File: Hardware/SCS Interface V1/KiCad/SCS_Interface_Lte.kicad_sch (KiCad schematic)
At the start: 23 parts, among them J1 SCS, J2 Conn_01x04, Q1 MMBTA06, Q2 MMBTA06

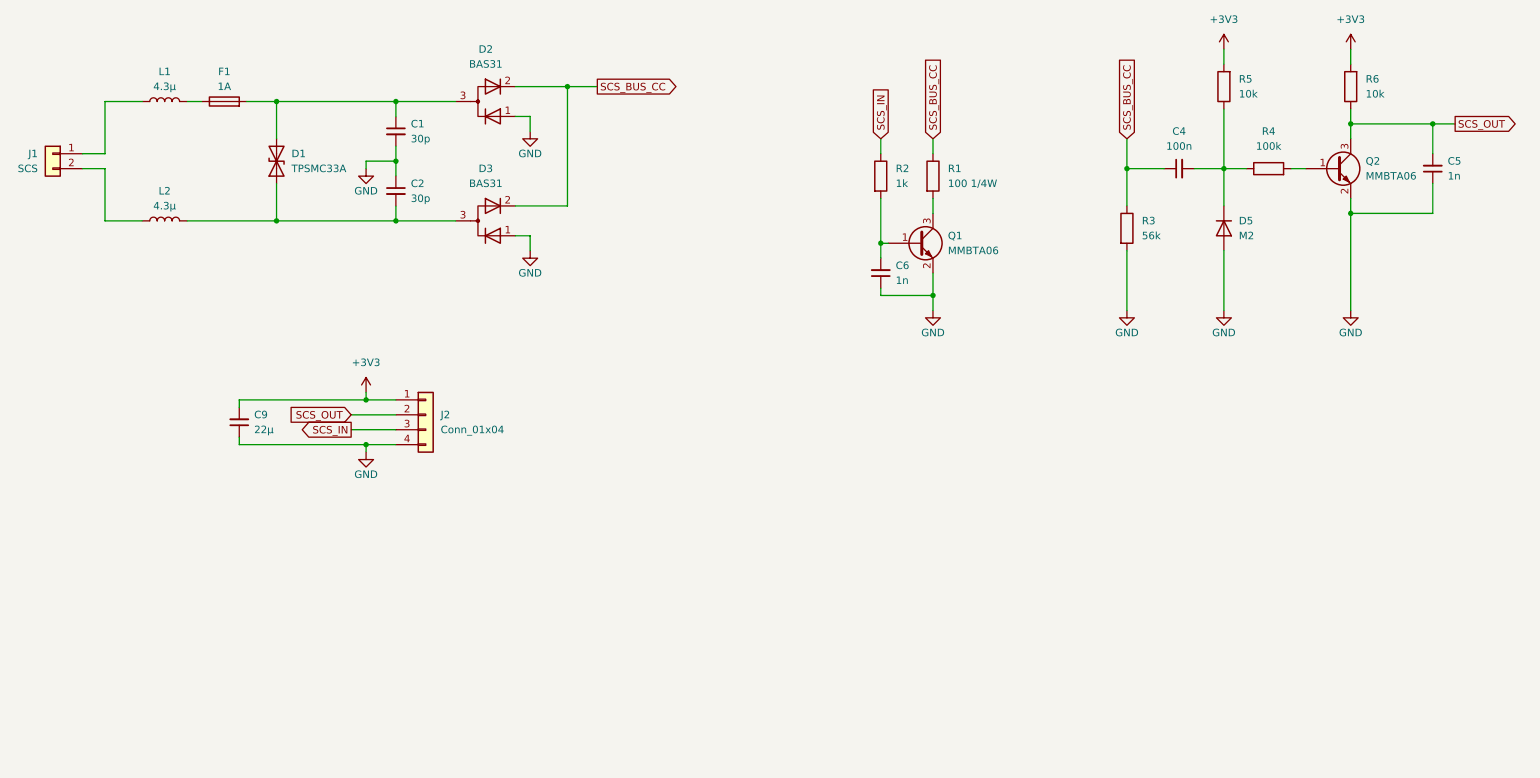
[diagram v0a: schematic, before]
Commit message: Update PCB after first pcb build
- Replace input detection
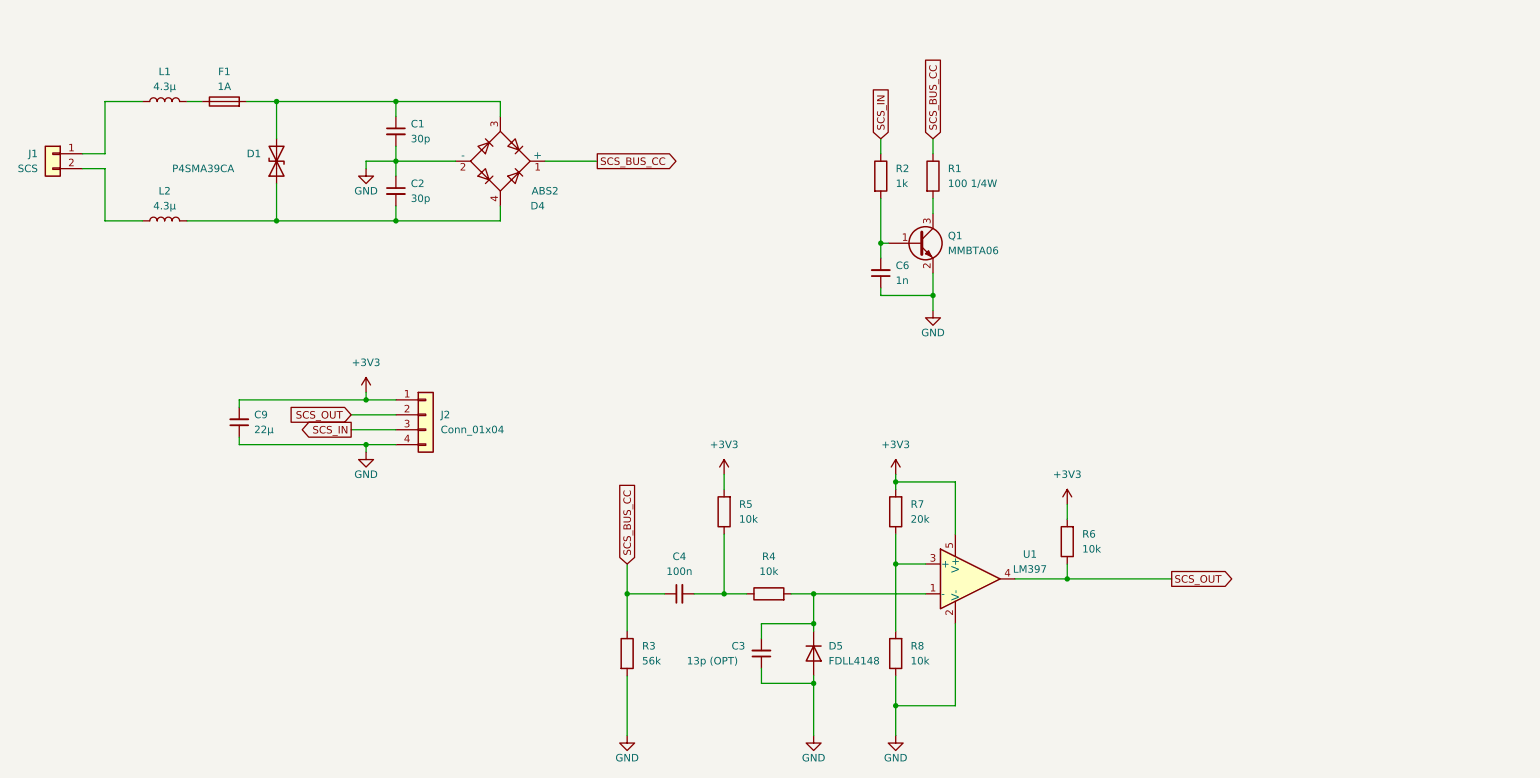
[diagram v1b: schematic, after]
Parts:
- removed C5: 1n, Capacitor_SMD:C_0805_2012Metric, symbol Device:C_Small
- removed D2, D3: BAS31, Package_TO_SOT_SMD:SOT-23, symbol Device:D_Dual_Series_AKC_Parallel
- removed Q2: MMBTA06, Package_TO_SOT_SMD:SOT-23, symbol Transistor_BJT:2SC4213
- added C3: 13p (OPT), Capacitor_SMD:C_0805_2012Metric, symbol Device:C_Small
- added D4: ABS2, Diode_SMD:Diode_Bridge_Diotec_ABS, symbol Diode_Bridge:ABS2
- added R7: 20k, Resistor_SMD:R_0805_2012Metric, symbol Device:R
- added R8: 10k, Resistor_SMD:R_0805_2012Metric, symbol Device:R
- added U1: LM397, Package_TO_SOT_SMD:SOT-23-5, symbol Comparator:LM397
- D1: value TPSMC33A -> P4SMA39CA; footprint Diode_SMD:D_SMC -> Diode_SMD:D_SMA
- D5: value M2 -> FDLL4148; footprint Diode_SMD:D_SMA -> Diode_SMD:D_MiniMELF; Prix 0.121 -> 0.09; Ref constructeurs SS13 -> FDLL4148-D87Z
- J1: footprint TerminalBlock_Phoenix:TerminalBlock_Phoenix_MKDS-1,5-2_1x02_P5.00mm_Horizontal -> TerminalBlock_Phoenix:TerminalBlock_Phoenix_MKDS-1,5-2_1x02_P5.00mm_Horizontal_PNP
- R4: value 100k -> 10k
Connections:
- net +3V3: now also R7.2, U1.5 (V+)
- net GND: now also C3.1, D4.2 (-), R8.1, U1.2 (V-)
- net SCS_BUS_CC: now also D4.1 (+)
- net SCS_OUT: now also U1.4
- net at R4.2: now also D5.1 (K), C3.2, U1.1 (-)
- net at C1.1, D1.2 (A2), F1.2: now also D4.3
- net at C2.2, D1.1 (A1), L2.2: now also D4.4
- net at C4.2, R4.1, R5.1: no longer D5.1 (K)
- new net: R7.1, R8.2, U1.3 (+)
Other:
- moved on the sheet: C4, D5, R3, R4, R5, R6
